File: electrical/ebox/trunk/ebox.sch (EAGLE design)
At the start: 158 parts, among them IC1 MAX3221CUE, IC10 SN74LVC1G125, IC11 MAX3221CUE, IC12 INA170, IC13 SN74LVC1G125, IC14 SN74LVC1G125, IC15 MAX3221CUE, IC16 MCP170333MB, IC17 SN74LVC1G125, IC18 SN74LVC1G125, IC19 74ALS04D, IC2 LT3652, IC3 XMEGA128A1, IC4 LT1161, IC5 SN74LVC1G125, IC6 SN74LVC1G125, IC7 MAX3221CUE, IC8 INA170, IC9 SN74LVC1G125, Q1 FDD4141TO252, U1 BLUETOOTH-RN42, U2 D2523T_, X1 7381-3PG-300, X10 DEANS-MALE, X11 B4B-ZR, X12 DEANS-MALE, X13 B4B-ZR, X14 22-23-2021, X15 DEANS-FEMALE, X16 DEANS-FEMALE, X17 USB_A, X2 7381-3PG-300, X3 7381-2PG-300, X4 17984-7PG-300, X5 17984-7PG-300, X6 17984-7PG-300, X7 17984-7PG-300, X8 22-23-2031, X9 22-23-2031

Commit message: Fixed sensor routing, couple of other things.
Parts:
- added C22: 10uF, rcl:C-USC0805
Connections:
- net +12V: now also C22.1
- net GND: now also C22.2
- net GPIO1A: now also IC3.PE0; no longer IC3.PD0
- net GPIO1B: now also IC3.PE1; no longer IC3.PB3, IC3.PD1
- net GPIO2A: now also IC3.PE4; no longer IC3.PD4
- net GPIO2B: now also IC3.PB3, IC3.PE5; no longer IC3.PD5
- net GPIO3A: now also IC3.PD0; no longer IC3.PE0
- net GPIO3B: now also IC3.PD1; no longer IC3.PE1
- net GPIO4A: now also IC3.PD4; no longer IC3.PE4
- net GPIO4B: now also IC3.PD5; no longer IC3.PE5
- net RX1_TTL: now also IC3.PE2; no longer IC3.PD2
- net RX2_TTL: now also IC3.PE6; no longer IC3.PD6
- net RX3_TTL: now also IC3.PD2; no longer IC3.PE2
- net RX4_TTL: now also IC3.PD6; no longer IC3.PE6
- net TX1_TTL: now also IC3.PE3; no longer IC3.PD3
- net TX2_TTL: now also IC3.PE7; no longer IC3.PD7
- net TX3_TTL: now also IC3.PD3; no longer IC3.PE3
- net TX4_TTL: now also IC3.PD7; no longer IC3.PE7

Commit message: More routing finished, under 100 airwires.
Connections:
- net N$17 renamed 3ROU
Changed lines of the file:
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@@
 </segment>
 </net>
-<net name="N$17" class="0">
+<net name="3ROU" class="0">
 <segment>
 <pinref part="IC4" gate="G$1" pin="G1"/>

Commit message: All high power routing is sufficient.  Tuning routing on digital lines.
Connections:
- net !CHRG: now also IC3.PJ1; no longer IC3.PJ3
- net !CHRG_FAULT: now also IC3.PJ0; no longer IC3.PJ2
- net !EN232_1: now also IC19D.I; no longer IC19A.I
- net !EN232_2: now also IC19C.I; no longer IC19B.I
- net !EN232_3: now also IC19B.I; no longer IC19C.I
- net !EN232_4: now also IC19A.I; no longer IC19D.I
- net BATT_CURR_IN: now also IC3.PB6; no longer IC3.PA0
- net BATT_CURR_OUT: now also IC3.PB7; no longer IC3.PA1
- net BATT_TEMP: now also IC3.PB5; no longer IC3.PA2
- net BATT_VSENSE: now also IC3.PB4; no longer IC3.PA3
- net BT_CTS: now also IC3.PF7; no longer IC3.PF4
- net BT_STATUS: now also IC3.PF4; no longer IC3.PF7
- net EN232_1: now also IC19D.O; no longer IC19A.O
- net EN232_2: now also IC19C.O; no longer IC19B.O
- net EN232_3: now also IC19B.O; no longer IC19C.O
- net EN232_4: now also IC19A.O; no longer IC19D.O
- net GPIO1A: now also IC3.PA0, IC3.PE5; no longer IC3.PB0, IC3.PE0
- net GPIO1B: now also IC3.PA1, IC3.PE4; no longer IC3.PB1, IC3.PE1
- net GPIO2A: now also IC3.PA2, IC3.PE1; no longer IC3.PB2, IC3.PE4
- net GPIO2B: now also IC3.PA3, IC3.PE0; no longer IC3.PB3, IC3.PE5
- net GPIO3A: now also IC3.PA4, IC3.PD5; no longer IC3.PB4, IC3.PD0
- net GPIO3B: now also IC3.PA5, IC3.PD4; no longer IC3.PB5, IC3.PD1
- net GPIO4A: now also IC3.PA6, IC3.PD1; no longer IC3.PB6, IC3.PD4
- net GPIO4B: now also IC3.PA7, IC3.PD0; no longer IC3.PB7, IC3.PD5
- net PWR_CTL: now also IC3.PJ3; no longer IC3.PH1
- net PWR_SENSE: now also IC3.PJ2; no longer IC3.PH2
- net RX1_TTL: now also IC3.PE6; no longer IC3.PE2
- net RX2_TTL: now also IC3.PE2; no longer IC3.PE6
- net RX3_TTL: now also IC3.PD6; no longer IC3.PD2
- net RX4_TTL: now also IC3.PD2; no longer IC3.PD6
- net TX1_TTL: now also IC3.PE7; no longer IC3.PE3
- net TX2_TTL: now also IC3.PE3; no longer IC3.PE7
- net TX3_TTL: now also IC3.PD7; no longer IC3.PD3
- net TX4_TTL: now also IC3.PD3; no longer IC3.PD7
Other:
- moved on the sheet: IC19A, IC19B, IC19C, IC19D

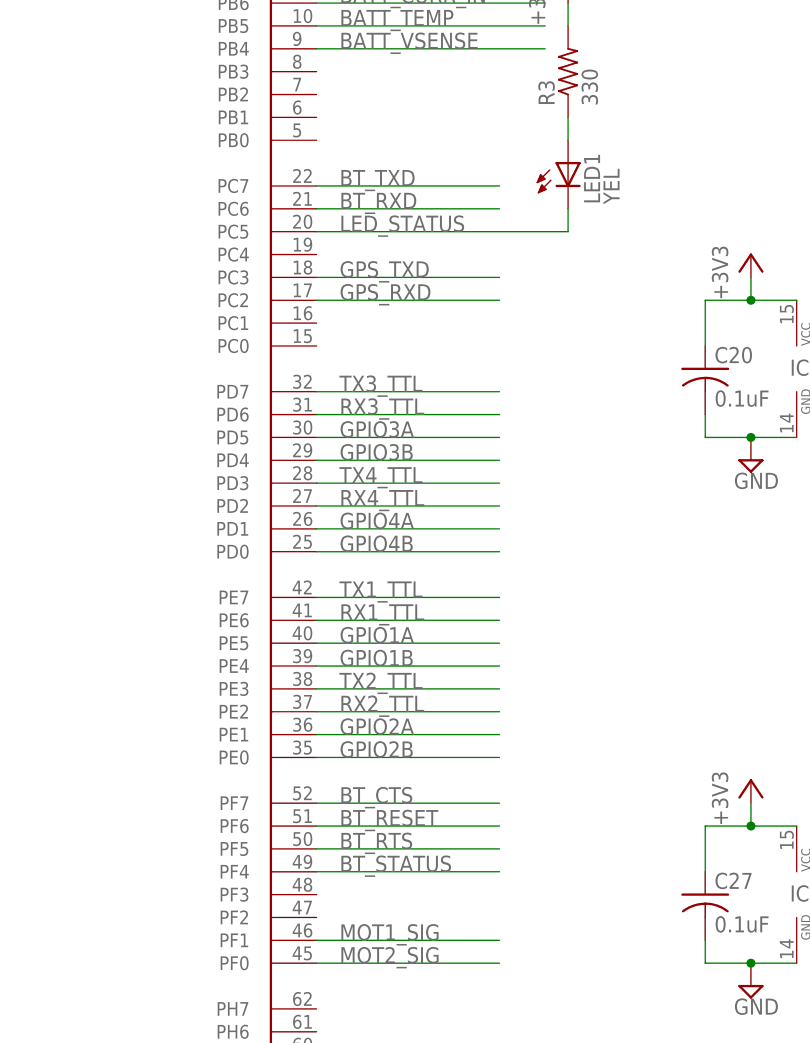
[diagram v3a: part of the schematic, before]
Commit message: Almost all digital routing completed and checked.  Need to do pwr ctrl and enable lines.
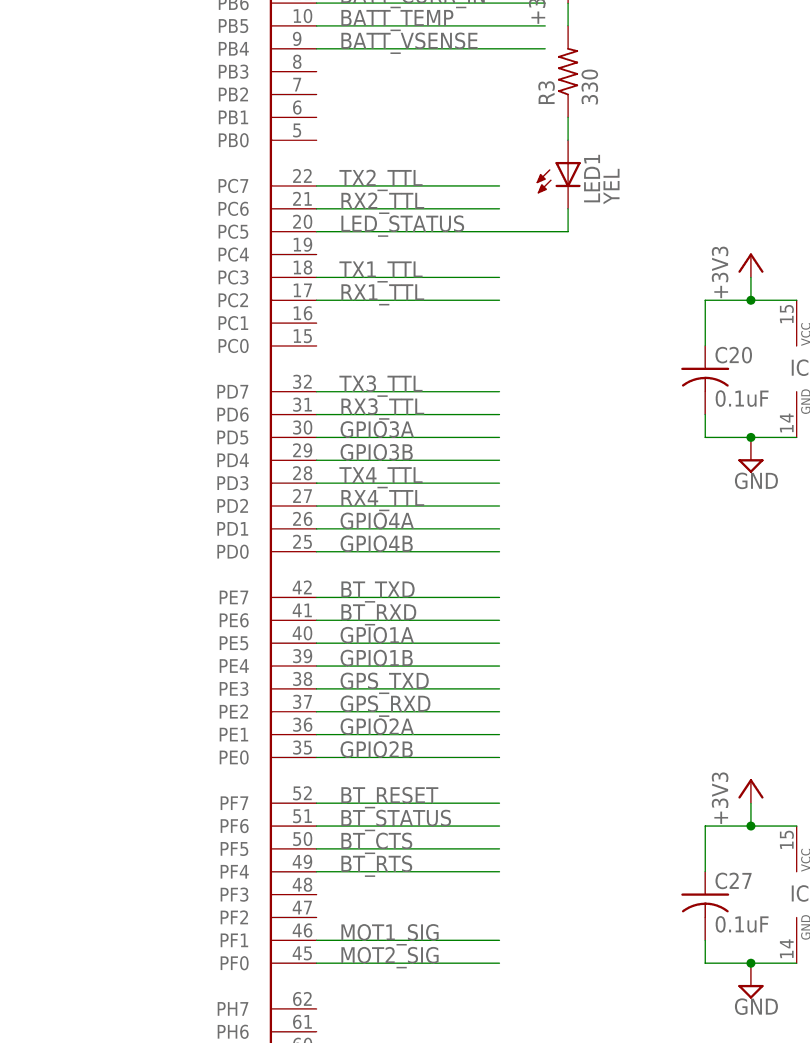
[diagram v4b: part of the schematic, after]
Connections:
- net BT_CTS: now also IC3.PF5; no longer IC3.PF7
- net BT_RESET: now also IC3.PF7; no longer IC3.PF6
- net BT_RTS: now also IC3.PF4; no longer IC3.PF5
- net BT_RXD: now also IC3.PE6; no longer IC3.PC6
- net BT_STATUS: now also IC3.PF6; no longer IC3.PF4
- net BT_TXD: now also IC3.PE7; no longer IC3.PC7
- net GPS_RXD: now also IC3.PE2; no longer IC3.PC2
- net GPS_TXD: now also IC3.PE3; no longer IC3.PC3
- net RX1_TTL: now also IC3.PC2; no longer IC3.PE6
- net RX2_TTL: now also IC3.PC6; no longer IC3.PE2
- net TX1_TTL: now also IC3.PC3; no longer IC3.PE7
- net TX2_TTL: now also IC3.PC7; no longer IC3.PE3
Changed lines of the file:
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@@
 </segment>
 <segment>
-<wire x1="111.76" y1="314.96" x2="132.08" y2="314.96" width="0.1524" layer="91"/>
-<label x="114.3" y="314.96" size="1.778" layer="95"/>
-<pinref part="IC3" gate="G$1" pin="PE7"/>
+<wire x1="111.76" y1="350.52" x2="132.08" y2="350.52" width="0.1524" layer="91"/>
+<label x="114.3" y="350.52" size="1.778" layer="95"/>
+<pinref part="IC3" gate="G$1" pin="PC3"/>
 </segment>
 </net>
@@
 </segment>
 <segment>
-<wire x1="111.76" y1="312.42" x2="132.08" y2="312.42" width="0.1524" layer="91"/>
-<label x="114.3" y="312.42" size="1.778" layer="95"/>
-<pinref part="IC3" gate="G$1" pin="PE6"/>
+<wire x1="111.76" y1="347.98" x2="132.08" y2="347.98" width="0.1524" layer="91"/>
+<label x="114.3" y="347.98" size="1.778" layer="95"/>
+<pinref part="IC3" gate="G$1" pin="PC2"/>
 </segment>
 </net>
@@
 <net name="GPS_RXD" class="0">
 <segment>
-<pinref part="IC3" gate="G$1" pin="PC2"/>
-<wire x1="111.76" y1="347.98" x2="132.08" y2="347.98" width="0.1524" layer="91"/>
-<label x="114.3" y="347.98" size="1.778" layer="95"/>
-</segment>
-<segment>
 <pinref part="U2" gate="G$1" pin="TX"/>
 <wire x1="500.38" y1="175.26" x2="515.62" y2="175.26" width="0.1524" layer="91"/>
 <label x="502.92" y="175.26" size="1.778" layer="95"/>
 </segment>
+<segment>
+<wire x1="111.76" y1="302.26" x2="132.08" y2="302.26" width="0.1524" layer="91"/>
+<label x="114.3" y="302.26" size="1.778" layer="95"/>
+<pinref part="IC3" gate="G$1" pin="PE2"/>
+</segment>
 </net>
 <net name="GPS_TXD" class="0">
-<segment>
-<pinref part="IC3" gate="G$1" pin="PC3"/>
-<wire x1="111.76" y1="350.52" x2="132.08" y2="350.52" width="0.1524" layer="91"/>
-<label x="114.3" y="350.52" size="1.778" layer="95"/>
-</segment>
 <segment>
 <pinref part="U2" gate="G$1" pin="RX"/>
@@
 <label x="502.92" y="172.72" size="1.778" layer="95"/>
 </segment>
+<segment>
+<wire x1="111.76" y1="304.8" x2="132.08" y2="304.8" width="0.1524" layer="91"/>
+<label x="114.3" y="304.8" size="1.778" layer="95"/>
+<pinref part="IC3" gate="G$1" pin="PE3"/>
+</segment>
 </net>
 <net name="BT_RXD" class="0">
-<segment>
-<pinref part="IC3" gate="G$1" pin="PC6"/>
-<wire x1="111.76" y1="358.14" x2="132.08" y2="358.14" width="0.1524" layer="91"/>
-<label x="114.3" y="358.14" size="1.778" layer="95"/>
-</segment>
 <segment>
 <pinref part="U1" gate="G$1" pin="UARTTX"/>
@@
 <label x="50.8" y="187.96" size="1.778" layer="95"/>
 </segment>
+<segment>
+<wire x1="111.76" y1="312.42" x2="132.08" y2="312.42" width="0.1524" layer="91"/>
+<label x="114.3" y="312.42" size="1.778" layer="95"/>
+<pinref part="IC3" gate="G$1" pin="PE6"/>
+</segment>
 </net>
 <net name="BT_TXD" class="0">
-<segment>
-<pinref part="IC3" gate="G$1" pin="PC7"/>
-<wire x1="111.76" y1="360.68" x2="132.08" y2="360.68" width="0.1524" layer="91"/>
-<label x="114.3" y="360.68" size="1.778" layer="95"/>
-</segment>
 <segment>
 <pinref part="U1" gate="G$1" pin="UARTRX"/>
@@
 <label x="50.8" y="190.5" size="1.778" layer="95"/>
 </segment>
+<segment>
+<wire x1="111.76" y1="314.96" x2="132.08" y2="314.96" width="0.1524" layer="91"/>
+<label x="114.3" y="314.96" size="1.778" layer="95"/>
+<pinref part="IC3" gate="G$1" pin="PE7"/>
+</segment>
 </net>
 <net name="RX2_TTL" class="0">
@@
 </segment>
 <segment>
-<wire x1="111.76" y1="302.26" x2="132.08" y2="302.26" width="0.1524" layer="91"/>
-<label x="114.3" y="302.26" size="1.778" layer="95"/>
-<pinref part="IC3" gate="G$1" pin="PE2"/>
+<wire x1="111.76" y1="358.14" x2="132.08" y2="358.14" width="0.1524" layer="91"/>
+<label x="114.3" y="358.14" size="1.778" layer="95"/>
+<pinref part="IC3" gate="G$1" pin="PC6"/>
 </segment>
 </net>
@@
 </segment>
 <segment>
-<wire x1="111.76" y1="304.8" x2="132.08" y2="304.8" width="0.1524" layer="91"/>
-<label x="114.3" y="304.8" size="1.778" layer="95"/>
-<pinref part="IC3" gate="G$1" pin="PE3"/>
+<wire x1="111.76" y1="360.68" x2="132.08" y2="360.68" width="0.1524" layer="91"/>
+<label x="114.3" y="360.68" size="1.778" layer="95"/>
+<pinref part="IC3" gate="G$1" pin="PC7"/>
 </segment>
 </net>
@@
 </segment>
 <segment>
-<pinref part="IC3" gate="G$1" pin="PF6"/>
-<wire x1="111.76" y1="289.56" x2="132.08" y2="289.56" width="0.1524" layer="91"/>
-<label x="114.3" y="289.56" size="1.778" layer="95"/>
+<wire x1="111.76" y1="292.1" x2="132.08" y2="292.1" width="0.1524" layer="91"/>
+<label x="114.3" y="292.1" size="1.778" layer="95"/>
+<pinref part="IC3" gate="G$1" pin="PF7"/>
 </segment>
 </net>
@@
 </segment>
 <segment>
-<wire x1="111.76" y1="284.48" x2="132.08" y2="284.48" width="0.1524" layer="91"/>
-<label x="114.3" y="284.48" size="1.778" layer="95"/>
-<pinref part="IC3" gate="G$1" pin="PF4"/>
+<wire x1="111.76" y1="289.56" x2="132.08" y2="289.56" width="0.1524" layer="91"/>
+<label x="114.3" y="289.56" size="1.778" layer="95"/>
+<pinref part="IC3" gate="G$1" pin="PF6"/>
 </segment>
 </net>
@@
 </segment>
 <segment>
-<pinref part="IC3" gate="G$1" pin="PF5"/>
-<wire x1="111.76" y1="287.02" x2="132.08" y2="287.02" width="0.1524" layer="91"/>
-<label x="114.3" y="287.02" size="1.778" layer="95"/>
+<wire x1="111.76" y1="284.48" x2="132.08" y2="284.48" width="0.1524" layer="91"/>
+<label x="114.3" y="284.48" size="1.778" layer="95"/>
+<pinref part="IC3" gate="G$1" pin="PF4"/>
 </segment>
 </net>
@@
 </segment>
 <segment>
-<wire x1="111.76" y1="292.1" x2="132.08" y2="292.1" width="0.1524" layer="91"/>
-<label x="114.3" y="292.1" size="1.778" layer="95"/>
-<pinref part="IC3" gate="G$1" pin="PF7"/>
-</segment>
-</net>
+<wire x1="111.76" y1="287.02" x2="132.08" y2="287.02" width="0.1524" layer="91"/>
+<label x="114.3" y="287.02" size="1.778" layer="95"/>
+<pinref part="IC3" gate="G$1" pin="PF5"/>
+</segment>
+</net>

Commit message: Added water sensor connection.
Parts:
- added R32: 1K, rcl:R-US_R0805
- added X18: 22-23-2021, con-molex:22-23-2021
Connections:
- new net N$17: IC3.PB3, R32.1
- new net WATER_SENSE: R32.2, X18-1.S
- net GND: now also X18-2.S
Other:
- moved on the sheet: LED1, R3
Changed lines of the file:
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@@
 <setting verticaltext="up"/>
 </settings>
-<grid distance="0.1" unitdist="inch" unit="inch" style="lines" multiple="1" display="no" altdistance="0.01" altunitdist="inch" altunit="inch"/>
+<grid distance="0.1" unitdist="inch" unit="inch" style="lines" multiple="1" display="yes" altdistance="0.01" altunitdist="inch" altunit="inch"/>
 <layers>
 <layer number="1" name="Top" color="4" fill="1" visible="no" active="no"/>
@@
 <part name="C22" library="rcl" deviceset="C-US" device="C0805" value="10uF"/>
 <part name="SUPPLY53" library="supply2" deviceset="GND" device=""/>
+<part name="X18" library="con-molex" deviceset="22-23-2021" device="">
+<attribute name="MF" value="MOLEX"/>
+<attribute name="MPN" value="22-23-2021"/>
+<attribute name="OC_FARNELL" value="1462926"/>
+<attribute name="OC_NEWARK" value="25C3832"/>
+</part>
+<part name="SUPPLY54" library="supply2" deviceset="GND" device=""/>
+<part name="R32" library="rcl" deviceset="R-US_" device="R0805" value="1K"/>
 </parts>
 <sheets>
@@
 <instance part="R2" gate="G$1" x="53.34" y="414.02" rot="R90"/>
 <instance part="+3V4" gate="G$1" x="53.34" y="424.18"/>
-<instance part="LED1" gate="G$1" x="139.7" y="363.22"/>
-<instance part="R3" gate="G$1" x="139.7" y="373.38" rot="R90"/>
-<instance part="+3V5" gate="G$1" x="139.7" y="383.54"/>
+<instance part="LED1" gate="G$1" x="147.32" y="363.22"/>
+<instance part="R3" gate="G$1" x="147.32" y="373.38" rot="R90"/>
+<instance part="+3V5" gate="G$1" x="147.32" y="383.54"/>
 <instance part="S1" gate="G$1" x="76.2" y="99.06"/>
 <instance part="S2" gate="G$1" x="132.08" y="243.84"/>
@@
 <instance part="C22" gate="G$1" x="401.32" y="411.48"/>
 <instance part="SUPPLY53" gate="GND" x="401.32" y="401.32"/>
+<instance part="X18" gate="-1" x="497.84" y="96.52" rot="MR0"/>
+<instance part="X18" gate="-2" x="497.84" y="93.98" rot="MR0"/>
+<instance part="SUPPLY54" gate="GND" x="523.24" y="91.44"/>
+<instance part="R32" gate="G$1" x="119.38" y="373.38" smashed="yes">
+<attribute name="NAME" x="118.11" y="371.8814" size="1.778" layer="95" rot="R180"/>
+<attribute name="VALUE" x="120.65" y="370.078" size="1.778" layer="96"/>
+</instance>
 </instances>
 <busses>
@@
 <wire x1="401.32" y1="403.86" x2="401.32" y2="406.4" width="0.1524" layer="91"/>
 </segment>
+<segment>
+<pinref part="X18" gate="-2" pin="S"/>
+<wire x1="500.38" y1="93.98" x2="523.24" y2="93.98" width="0.1524" layer="91"/>
+<pinref part="SUPPLY54" gate="GND" pin="GND"/>
+</segment>
 </net>
 <net name="S1_12V" class="0">
@@
 <pinref part="+3V5" gate="G$1" pin="+3V3"/>
 <pinref part="R3" gate="G$1" pin="2"/>
-<wire x1="139.7" y1="381" x2="139.7" y2="378.46" width="0.1524" layer="91"/>
+<wire x1="147.32" y1="381" x2="147.32" y2="378.46" width="0.1524" layer="91"/>
 </segment>
 <segment>
@@
 <segment>
 <pinref part="IC3" gate="G$1" pin="PC5"/>
-<wire x1="111.76" y1="355.6" x2="139.7" y2="355.6" width="0.1524" layer="91"/>
+<wire x1="111.76" y1="355.6" x2="147.32" y2="355.6" width="0.1524" layer="91"/>
 <label x="114.3" y="355.6" size="1.778" layer="95"/>
 <pinref part="LED1" gate="G$1" pin="C"/>
-<wire x1="139.7" y1="355.6" x2="139.7" y2="358.14" width="0.1524" layer="91"/>
+<wire x1="147.32" y1="355.6" x2="147.32" y2="358.14" width="0.1524" layer="91"/>
 </segment>
 </net>
@@
 <segment>
 <pinref part="LED1" gate="G$1" pin="A"/>
-<wire x1="139.7" y1="365.76" x2="139.7" y2="368.3" width="0.1524" layer="91"/>
+<wire x1="147.32" y1="365.76" x2="147.32" y2="368.3" width="0.1524" layer="91"/>
 <pinref part="R3" gate="G$1" pin="1"/>
 </segment>
@@
 </segment>
 </net>
+<net name="WATER_SENSE" class="0">
+<segment>
+<pinref part="X18" gate="-1" pin="S"/>
+<wire x1="523.24" y1="96.52" x2="500.38" y2="96.52" width="0.1524" layer="91"/>
+<label x="502.92" y="96.52" size="1.778" layer="95"/>
+</segment>
+<segment>
+<wire x1="124.46" y1="373.38" x2="142.24" y2="373.38" width="0.1524" layer="91"/>
+<label x="124.46" y="373.38" size="1.778" layer="95"/>
+<pinref part="R32" gate="G$1" pin="2"/>
+</segment>
+</net>
+<net name="N$17" class="0">
+<segment>
+<pinref part="IC3" gate="G$1" pin="PB3"/>
+<pinref part="R32" gate="G$1" pin="1"/>
+<wire x1="114.3" y1="373.38" x2="111.76" y2="373.38" width="0.1524" layer="91"/>
+</segment>
+</net>

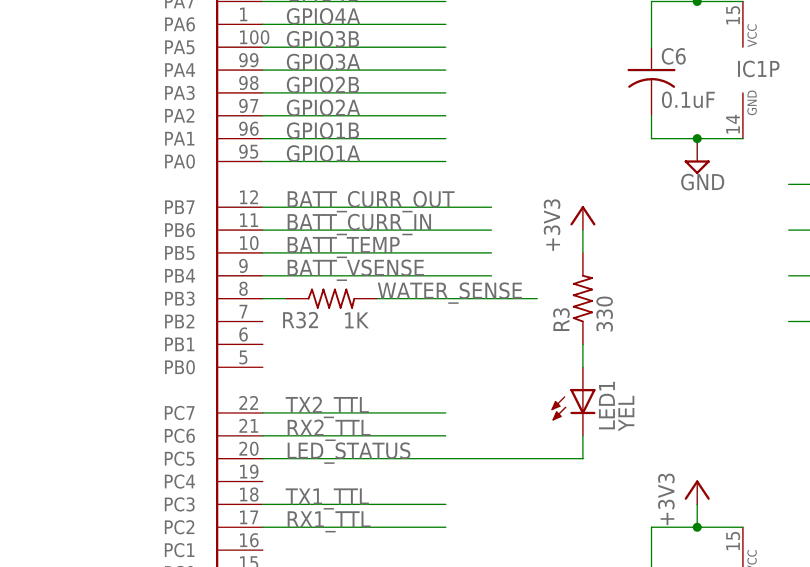
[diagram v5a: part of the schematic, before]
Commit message: Routed stuff up again.  Seem to have a ground plane partition to resolve.
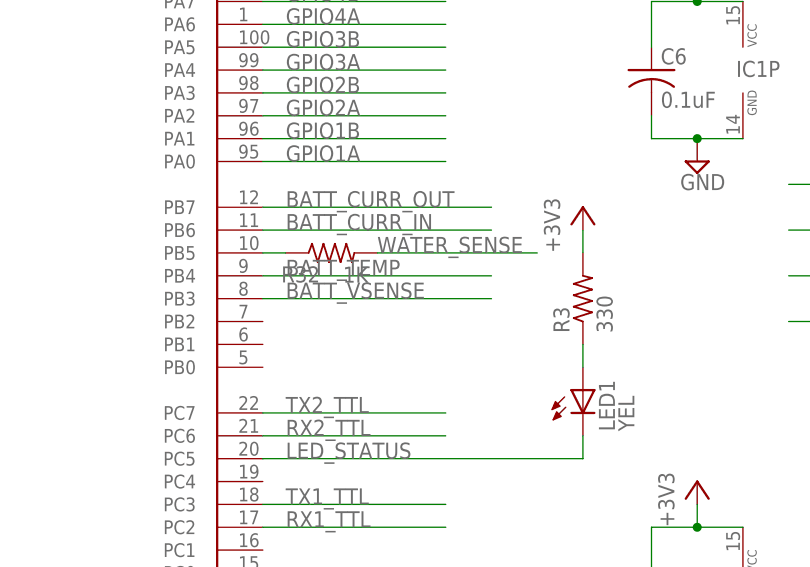
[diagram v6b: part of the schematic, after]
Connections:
- net BATT_TEMP: now also IC3.PB4; no longer IC3.PB5
- net BATT_VSENSE: now also IC3.PB3; no longer IC3.PB4
- net N$17: now also IC3.PB5; no longer IC3.PB3
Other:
- moved on the sheet: R32
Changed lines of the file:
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@@
 <setting verticaltext="up"/>
 </settings>
-<grid distance="0.1" unitdist="inch" unit="inch" style="lines" multiple="1" display="yes" altdistance="0.01" altunitdist="inch" altunit="inch"/>
+<grid distance="0.1" unitdist="inch" unit="inch" style="lines" multiple="1" display="no" altdistance="0.01" altunitdist="inch" altunit="inch"/>
 <layers>
 <layer number="1" name="Top" color="4" fill="1" visible="no" active="no"/>
@@
 <instance part="X18" gate="-2" x="497.84" y="93.98" rot="MR0"/>
 <instance part="SUPPLY54" gate="GND" x="523.24" y="91.44"/>
-<instance part="R32" gate="G$1" x="119.38" y="373.38" smashed="yes">
-<attribute name="NAME" x="118.11" y="371.8814" size="1.778" layer="95" rot="R180"/>
-<attribute name="VALUE" x="120.65" y="370.078" size="1.778" layer="96"/>
+<instance part="R32" gate="G$1" x="119.38" y="378.46" smashed="yes">
+<attribute name="NAME" x="118.11" y="376.9614" size="1.778" layer="95" rot="R180"/>
+<attribute name="VALUE" x="120.65" y="375.158" size="1.778" layer="96"/>
 </instance>
 </instances>
@@
 </segment>
 <segment>
-<wire x1="111.76" y1="378.46" x2="137.16" y2="378.46" width="0.1524" layer="91"/>
-<label x="114.3" y="378.46" size="1.778" layer="95"/>
-<pinref part="IC3" gate="G$1" pin="PB5"/>
+<wire x1="111.76" y1="375.92" x2="137.16" y2="375.92" width="0.1524" layer="91"/>
+<label x="114.3" y="375.92" size="1.778" layer="95"/>
+<pinref part="IC3" gate="G$1" pin="PB4"/>
 </segment>
 </net>
@@
 </segment>
 <segment>
-<wire x1="111.76" y1="375.92" x2="137.16" y2="375.92" width="0.1524" layer="91"/>
-<label x="114.3" y="375.92" size="1.778" layer="95"/>
-<pinref part="IC3" gate="G$1" pin="PB4"/>
+<wire x1="111.76" y1="373.38" x2="137.16" y2="373.38" width="0.1524" layer="91"/>
+<label x="114.3" y="373.38" size="1.778" layer="95"/>
+<pinref part="IC3" gate="G$1" pin="PB3"/>
 </segment>
 </net>
@@
 </segment>
 <segment>
-<wire x1="124.46" y1="373.38" x2="142.24" y2="373.38" width="0.1524" layer="91"/>
-<label x="124.46" y="373.38" size="1.778" layer="95"/>
+<wire x1="124.46" y1="378.46" x2="142.24" y2="378.46" width="0.1524" layer="91"/>
+<label x="124.46" y="378.46" size="1.778" layer="95"/>
 <pinref part="R32" gate="G$1" pin="2"/>
 </segment>
@@
 <net name="N$17" class="0">
 <segment>
-<pinref part="IC3" gate="G$1" pin="PB3"/>
+<pinref part="IC3" gate="G$1" pin="PB5"/>
 <pinref part="R32" gate="G$1" pin="1"/>
-<wire x1="114.3" y1="373.38" x2="111.76" y2="373.38" width="0.1524" layer="91"/>
+<wire x1="111.76" y1="378.46" x2="114.3" y2="378.46" width="0.1524" layer="91"/>
 </segment>
 </net>

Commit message: Cleaned up more stuff.  Just need to do final check and silkscreen work.
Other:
- moved on the sheet: C43, C44, C45, C46, IC12, IC8, LED1, R23, R25, R26, R27, R3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
